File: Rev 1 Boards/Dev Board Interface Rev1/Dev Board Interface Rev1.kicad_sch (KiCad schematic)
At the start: 0 parts

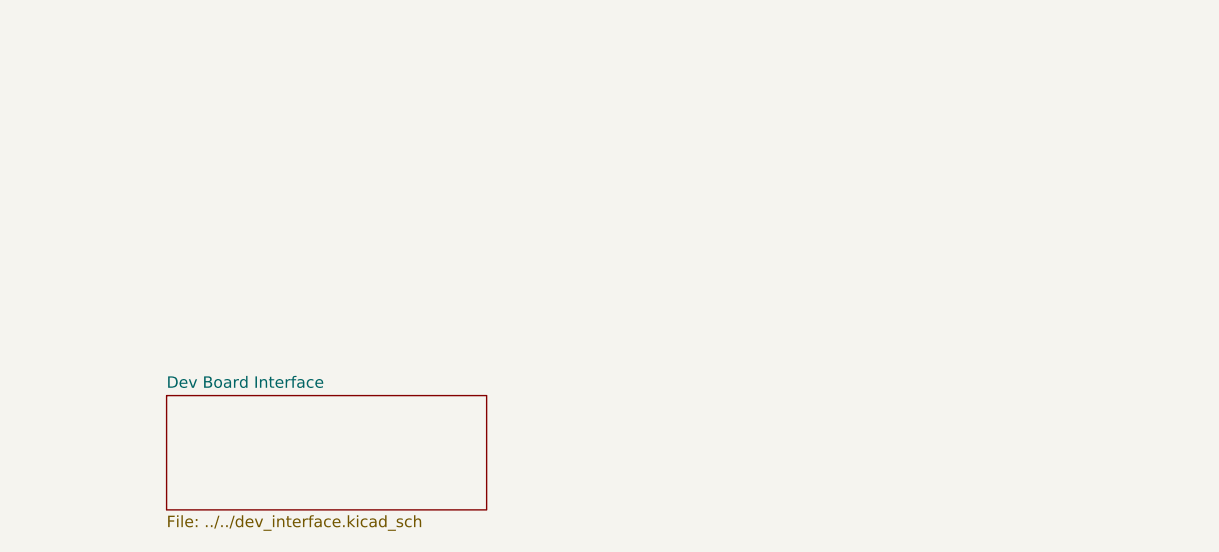
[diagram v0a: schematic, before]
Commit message: Created preliminary board layout for dev board interface pcb, pending review by Jed
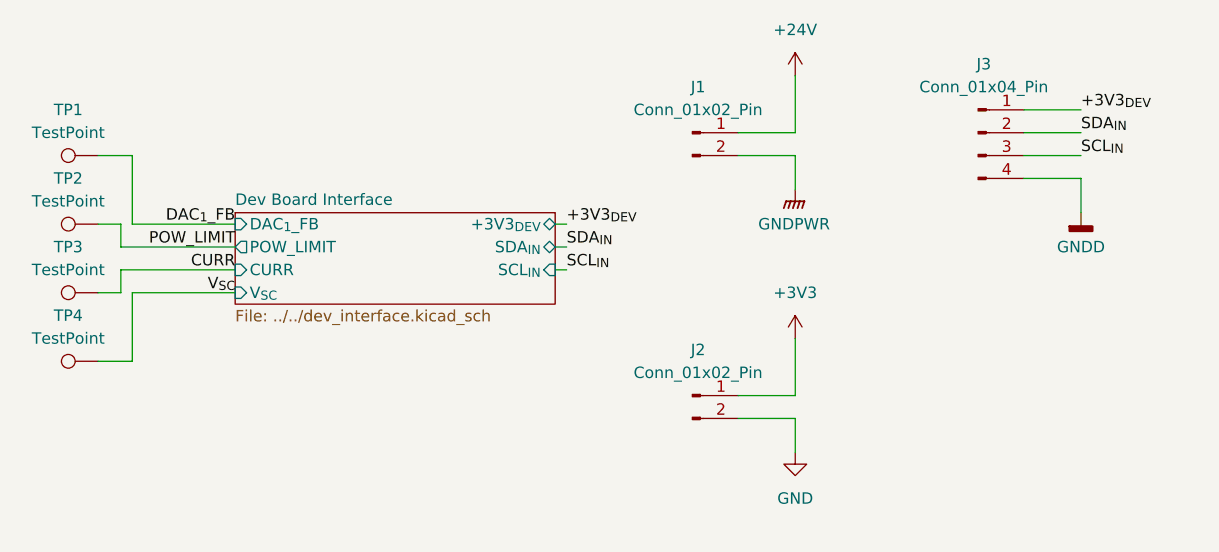
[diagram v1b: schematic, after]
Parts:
- added J1, J2: Conn_01x02_Pin, Connector:Banana_Jack_2Pin, symbol Connector:Conn_01x02_Pin
- added J3: Conn_01x04_Pin, Connector_JST:JST_GH_BM04B-GHS-TBT_1x04-1MP_P1.25mm_Vertical, symbol Connector:Conn_01x04_Pin
- added TP1, TP2, TP3, TP4: TestPoint, TestPoint:TestPoint_Bridge_Pitch2.0mm_Drill0.7mm, symbol Connector:TestPoint
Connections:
- new net +24V: J1.1 (Pin_1)
- new net +3V3: J2.1 (Pin_1)
- new net +3V3_{DEV}: J3.1 (Pin_1)
- new net CURR: TP3.1
- new net DAC_{1}_FB: TP1.1
- new net GND: J2.2 (Pin_2)
- new net GNDD: J3.4 (Pin_4)
- new net GNDPWR: J1.2 (Pin_2)
- new net POW_LIMIT: TP2.1
- new net SCL_{IN}: J3.3 (Pin_3)
- new net SDA_{IN}: J3.2 (Pin_2)
- new net V_{SC}: TP4.1
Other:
- sheet Dev Board Interface ports: added +3V3_{DEV}, CURR, DAC_{1}_FB, POW_LIMIT, SCL_{IN}, SDA_{IN}, V_{SC}; removed none
